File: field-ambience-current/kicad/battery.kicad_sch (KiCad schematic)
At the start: 10 parts, among them J4 SWD 1.27mm (SWCLK/GND/SWDIO), SW11 Reset 6mm SMD, SW12 BOOTSEL 6mm SMD (DNP for THT-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, U1 Raspberry_Pi_Pico2 (RP2350)

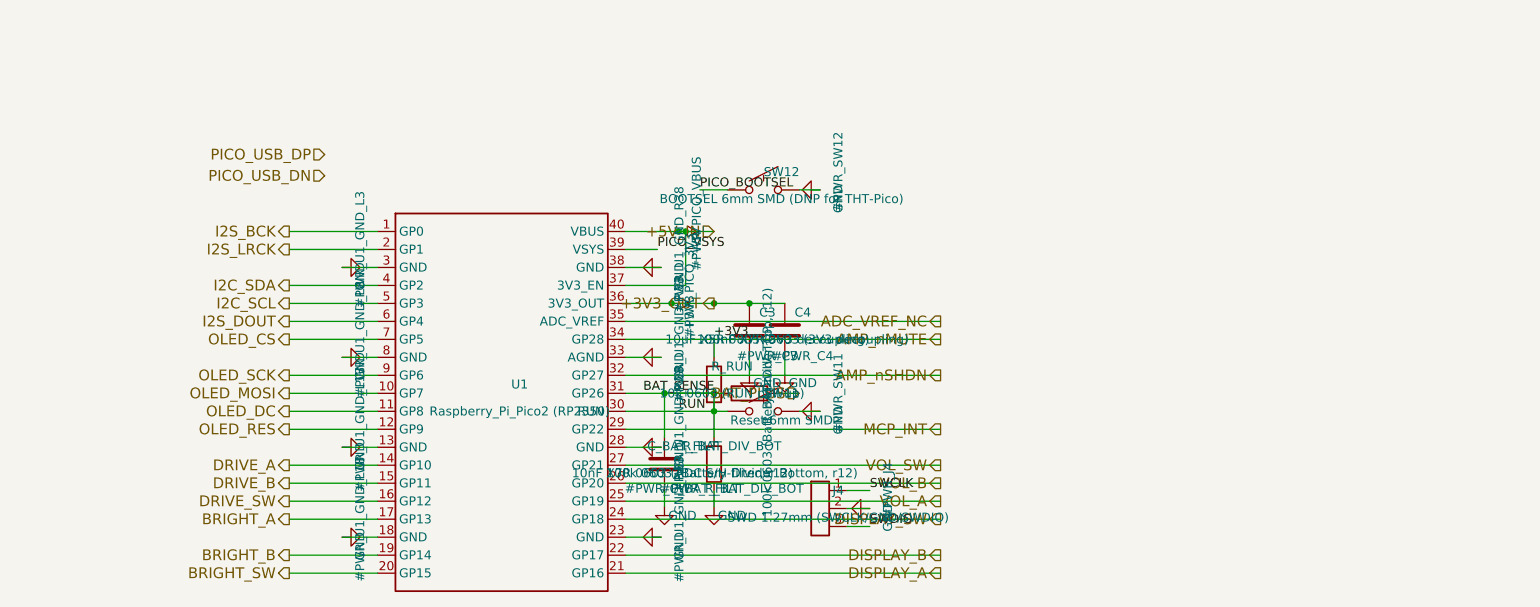
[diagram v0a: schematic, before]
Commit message: pcb(gen): r12-Sense + r9-Battery — KiCad-Generator vervollständigt
Zweite + dritte Hälfte von r10-B9/r7-B3. Bringt Generator vollständig in
Sync mit allen SPEC-Revisionen r9 (Battery-Add), r12 (Battery-Sense-HW),
r10-LED (LED1 auf PCA-Ch 10).

5 neue Library-Symbole (zwischen _pca9685pw_lib_symbol und
_rotary_encoder_switch_lib_symbol):
- _mcp73831_lib_symbol() — SOT-23-5, 5-pin Microchip-Charger
- _tps61089_lib_symbol() — QFN-12+ePAD, 13-pin TI-Boost
- _dmg2305ux_lib_symbol() — SOT-23, 3-pin P-MOSFET
- _inductor_lib_symbol() — Device:L, 2-pin
- _schottky_diode_lib_symbol() — Device:D_Schottky, 2-pin

Neuer Sheet 7 battery.kicad_sch (106 KB, 1848 Zeilen, paren-balanced):
- U7 MCP73831 LiPo-Charger 500mA via R21=2kΩ R_PROG, STAT→R_CHRG→LED_CHRG→+5V
- U8 TPS61089 Boost LiPo→5V mit L1 2.2µH + R23/R24 FB-Divider (200k/39k → ~4.92V)
- Q1 DMG2305UX P-MOS Power-Path (S=VBUS_USBC, D=+5V_OUT, G→R22 10kΩ pull-down)
- D3 SS34 Schottky zwischen BOOST_OUT und +5V_OUT (Reverse-Protect)
- J9 JST-PH-2P, C_BAT_IN/HF (22µF+100nF), C_BOOST_OUT/HF (22µF+100nF)
- Hier-I/O: VBUS_USBC ← (Power-Tree), BAT_PLUS → (Pico), +5V_OUT → (System-Rail)

r12-Sense in pico_sheet:
- GP26 STATUS_LED-Block entfernt (R19+LED1+GND-Flag weg, 0 hits in pico.kicad_sch)
- BAT_SENSE-Divider rein: R_BAT_DIV_TOP/BOT (100kΩ je), C_BAT_FILT (10nF)
- Hier-Input BAT_PLUS am Divider-Top

r12-Sense in mcp_sheet:
- GPA7 NC_GPA7 → USB_VBUS_SENSE mit R_VBUS_SENSE (10kΩ Series) + R_VBUS_PD
  (100kΩ Pull-Down) + hier-Input VBUS_USBC
- LED1 + R_LED_STATUS (390Ω 0603) auf PCA-Ch 10 (Pin 17, rechts) bei (130, 230)
- STATUS_LED_K Net-Label matched LED1-Kathode mit PCA-LED10-Pin
- NC-Loop reduziert auf LED11-LED15

power_tree_sheet:
- VBUS_USBC hier-Output (90° nach oben) am pre-fuse Rail-Tap bei (30.48, RAIL_Y-6)

root_sheet:
- Sheet 7 Battery-Block bei (30, 180) size 60×40 mit Pins VBUS_USBC/BAT_PLUS/+5V_OUT
- Existing Sheet-Blöcke erweitert: power_tree +VBUS_USBC out (90,95), pico +BAT_PLUS
  in (130,165), mcp +VBUS_USBC in 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
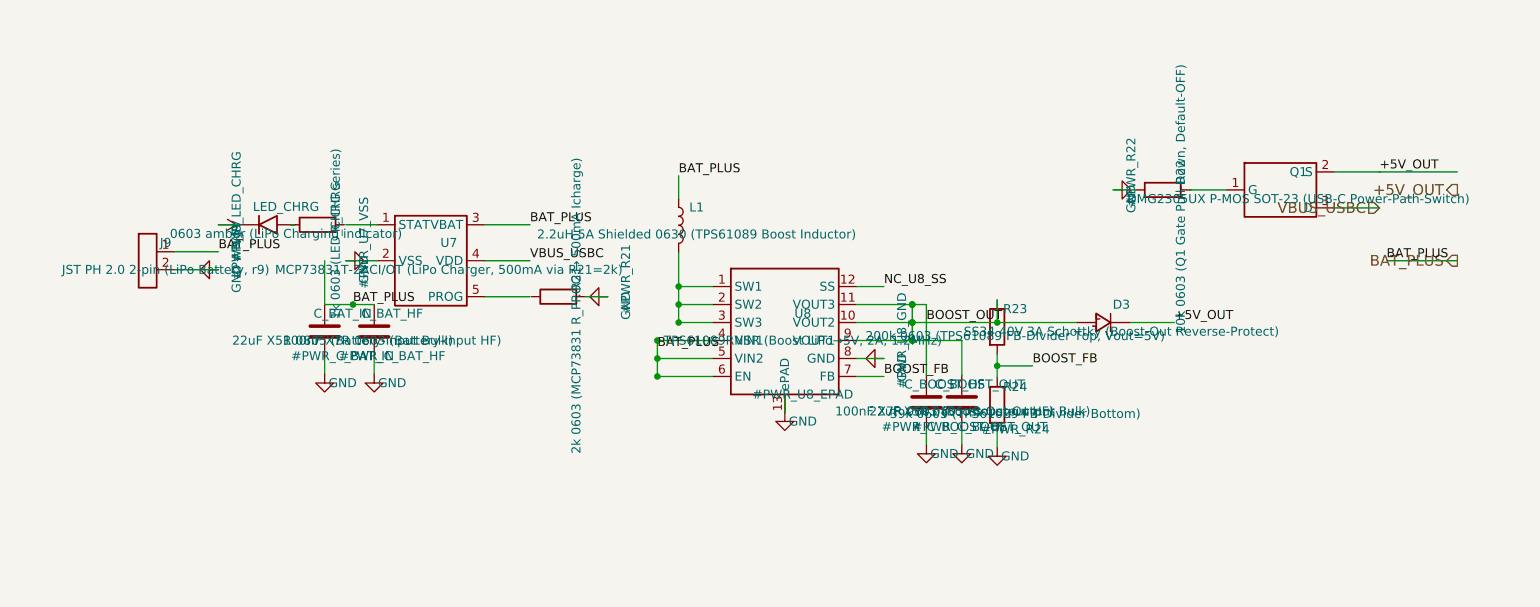
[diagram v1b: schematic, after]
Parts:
- removed C3: 10uF X5R 0805 (3V3 decoupling), Capacitor_SMD:C_0805_2012Metric, symbol Device:C
- removed C4: 100nF X7R 0603 (3V3 decoupling), Capacitor_SMD:C_0603_1608Metric, symbol Device:C
- removed C_BAT_FILT: 10nF X7R 0603 (ADC S/H filter, r12), Capacitor_SMD:C_0603_1608Metric, symbol Device:C
- removed J4: SWD 1.27mm (SWCLK/GND/SWDIO), Connector_PinHeader_1.27mm:PinHeader_1x03_P1.27mm_Vertical, symbol Connector:Conn_01x03
- removed R_BAT_DIV_BOT: 100k 0603 (Battery-Divider Bottom, r12), Resistor_SMD:R_0603_1608Metric, symbol Device:R
- removed R_BAT_DIV_TOP: 100k 0603 (Battery-Divider Top, r12), Resistor_SMD:R_0603_1608Metric, symbol Device:R
- removed R_RUN: 10k 0603 (RUN pull-up), Resistor_SMD:R_0603_1608Metric, symbol Device:R
- removed SW11: Reset 6mm SMD, Button_Switch_SMD:SW_SPST_TL3342, symbol Switch:SW_Push
- removed SW12: BOOTSEL 6mm SMD (DNP for THT-Pico), Button_Switch_SMD:SW_SPST_TL3342, symbol Switch:SW_Push
- removed U1: Raspberry_Pi_Pico2 (RP2350), MCU_Module:RPi_Pico_SMD_TH, symbol MCU:Pico2
- added C_BAT_HF: 100nF X7R 0603 (Battery-Input HF), Capacitor_SMD:C_0603_1608Metric, symbol Device:C
- added C_BAT_IN: 22uF X5R 0805 (Battery-Input Bulk), Capacitor_SMD:C_0805_2012Metric, symbol Device:C
- added C_BOOST_HF: 100nF X7R 0603 (Boost-Output HF), Capacitor_SMD:C_0603_1608Metric, symbol Device:C
- added C_BOOST_OUT: 22uF X5R 0805 (Boost-Output Bulk), Capacitor_SMD:C_0805_2012Metric, symbol Device:C
- added D3: SS34 40V 3A Schottky (Boost-Out Reverse-Protect), Diode_SMD:D_SMA, symbol Device:D_Schottky
- added J9: JST PH 2.0 2-pin (LiPo Battery, r9), Connector_JST:JST_PH_S2B-PH-SM4-TB_1x02-1MP_P2.00mm_Horizontal, symbol Connector:Conn_01x02
- added L1: 2.2uH 5A Shielded 0630 (TPS61089 Boost Inductor), Inductor_SMD:L_0630_6.0x6.0mm, symbol Device:L
- added LED_CHRG: 0603 amber (LiPo Charging indicator), LED_SMD:LED_0603_1608Metric, symbol Device:LED
- added Q1: DMG2305UX P-MOS SOT-23 (USB-C Power-Path-Switch), Package_TO_SOT_SMD:SOT-23, symbol Transistor_FET:DMG2305UX
- added R21: 2k 0603 (MCP73831 R_PROG → 500mA Icharge), Resistor_SMD:R_0603_1608Metric, symbol Device:R
- added R22: 10k 0603 (Q1 Gate Pull-Down, Default-OFF), Resistor_SMD:R_0603_1608Metric, symbol Device:R
- added R23: 200k 0603 (TPS61089 FB-Divider Top, Vout=5V), Resistor_SMD:R_0603_1608Metric, symbol Device:R
- added R24: 39k 0603 (TPS61089 FB-Divider Bottom), Resistor_SMD:R_0603_1608Metric, symbol Device:R
- added R_CHRG: 1k 0603 (LED_CHRG series), Resistor_SMD:R_0603_1608Metric, symbol Device:R
- added U7: MCP73831T-2ACI/OT (LiPo Charger, 500mA via R21=2k), Package_TO_SOT_SMD:SOT-23-5, symbol Battery:MCP73831
- added U8: TPS61089RNSR (Boost LiPo→5V, 2A, 1.2MHz), Package_DFN_QFN:VQFN-12-1EP_3x3mm_P0.5mm_EP1.5x1.5mm, symbol Regulator_Switching:TPS61089
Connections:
- net +5V: now also LED_CHRG.1 (K)
- net BAT_PLUS: now also C_BAT_HF.1, C_BAT_IN.1, J9.1 (Pin_1), L1.1, U7.3 (VBAT), U8.4 (VIN1), U8.5 (VIN2), U8.6 (EN)
- net GND: now also C_BAT_HF.2, C_BAT_IN.2, C_BOOST_HF.2, C_BOOST_OUT.2, J9.2 (Pin_2), R21.2, R22.1, R24.2, U7.2 (VSS), U8.13 (ePAD), U8.8 (GND)
- new net: L1.2, U8.1 (SW1), U8.2 (SW2), U8.3 (SW3)
- new net: Q1.1 (G), R22.2
- new net: LED_CHRG.2 (A), R_CHRG.1
- new net +5V_OUT: D3.1 (K), Q1.2 (S)
- new net BOOST_FB: R23.2, R24.1, U8.7 (FB)
- new net BOOST_OUT: C_BOOST_HF.1, C_BOOST_OUT.1, D3.2 (A), R23.1, U8.10 (VOUT2), U8.11 (VOUT3), U8.9 (VOUT1)
- new net NC_U8_SS: U8.12 (SS)
- new net VBUS_USBC: Q1.3 (D), U7.4 (VDD)
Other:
- title: Field Ambience PCB — Sheet 2: Pico 2 (RP2350) -> Field Ambience PCB — Sheet 7: Battery & Power-Path (r9 + r12)

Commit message: pcb(gen): kicad-Analyzer-Bugfixes (ERC: 8 errors→6, NT-001 33→16)
Schematic-Analyzer fand drei klassen von echten Connectivity-Bugs in den
beiden Generator-Catchup-Commits (50b5e02 + 0a3a740). Alle gefixt.

Bug 1: Label-Position 3mm neben Wire-Endpunkt → 33 dangling-pin-Nets
  - r10-LED PCA-pin-Labels (10 LEDs + 5 NC + STATUS_LED_K) saßen bei
    PCA_PIN_*_X±8 statt ±5 → keine 10 LEDs waren physisch an PCA9685
    connected. Fix: Labels auf Wire-Endpunkt verschoben.

Bug 2: Sub-mm-Gaps (0.19mm) zwischen Wires und Resistor-Pins
  - R rotation=90 horizontal hat pin1/pin2 bei sx±3.81 (X.19/X.81).
    Meine Wires endeten bei integer-mm → 0.19mm Gap = dangling.
  - Fixed: R_OE (mcp_sheet PCA-OE), R_VBUS_SENSE (mcp_sheet GPA7),
    R_CHRG (battery_sheet U7-STAT), R21 (battery_sheet U7-PROG).

Bug 3: Y-Inversion bei Q1 DMG2305UX P-MOS
  - KiCad-Symbol-local-Y ist invertiert zu Schematic-abs-Y. Meine
    q1_s_y und q1_d_y waren vertauscht → Q1.2 (S) auf +5V_OUT statt
    VBUS_USBC (SPEC-§2.2-violation!). Analyzer hat das korrekt
    gefangen. Fix: Y-Werte getauscht, S=VBUS_USBC ✓, D=+5V_OUT ✓.

Bug 4: Lokal-Label statt Hier-Label für Cross-Sheet-Nets
  - Lokale Labels mergen NICHT mit Hier-Labels im Analyzer-View
    (auch wenn KiCad-GUI das toleriert). Battery_sheet U7-VDD,
    U7-VBAT, U8-VIN, L1-top, Q1-D, D3-K, J9-pin1, C_BAT_IN waren
    alle mit lokalen Labels markiert → keine Cross-Sheet-Merge.
    Plus mcp_sheet PCA-side I²C-SCL/SDA.
  - Fix: alle zu hier_labels umgewandelt. I²C-Bus hat jetzt 4 Pins
    (U1+U2+R-Pullup+U6) statt 2 isolierte Sub-Nets.

Bug 5: +5V_OUT (Battery) mergt nicht mit System +5V
  - Hier-Label-Name "+5V_OUT" ≠ Power-Tree-Net-Name "+5V". Battery's
    +5V_OUT war ein isoliertes 2-pin Net (D3.K + Q1.D).
  - Fix: Bridge-Label "+5V_OUT" am existing Power-Tree→Pico-Wire
    (110, 50) im root_sheet. +5V hat jetzt 49 pins (war 47).

Bug 6: Redundante Edge-Hier-Labels in battery_sheet
  - Hatte standalone hier_labels bei (235, 70/80) zusätzlich zu de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
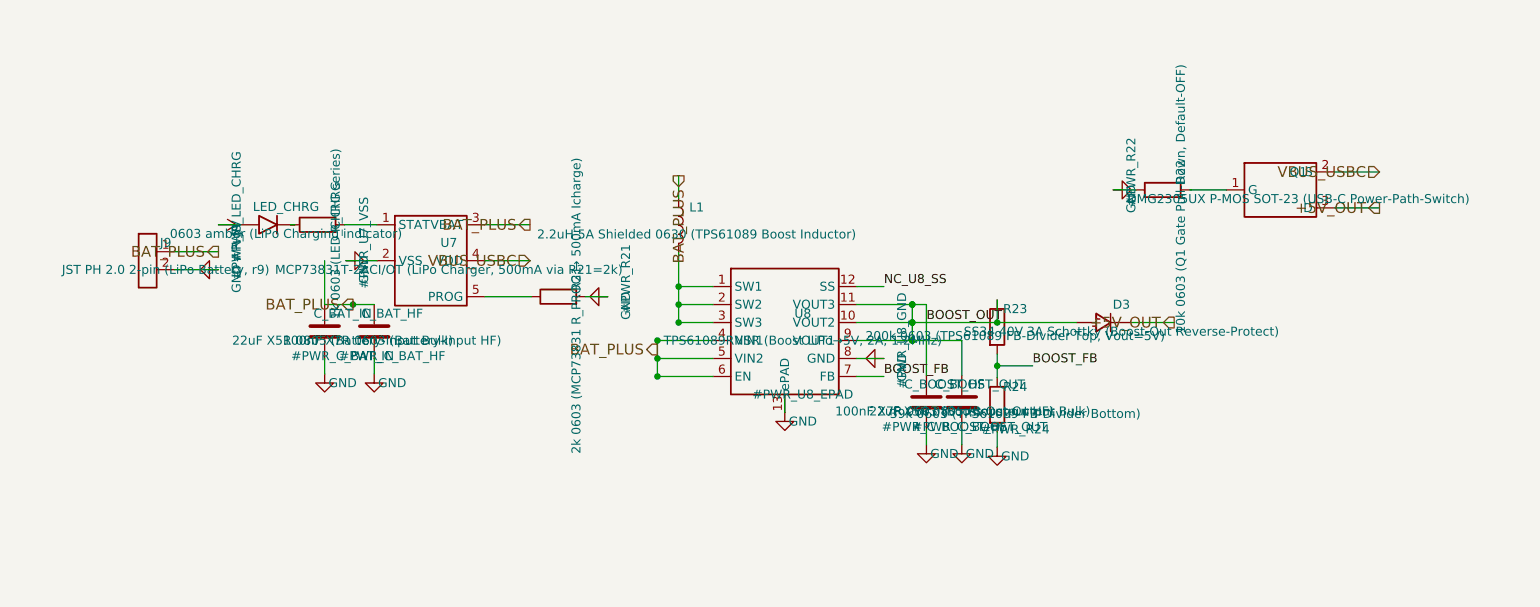
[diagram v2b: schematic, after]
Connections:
- net +5V: now also LED_CHRG.2 (A); no longer LED_CHRG.1 (K)
- net +5V_OUT: now also Q1.3 (D); no longer Q1.2 (S)
- net VBUS_USBC: now also Q1.2 (S); no longer Q1.3 (D)
- net at R21.1: now also U7.5 (PROG)
- net at R_CHRG.1: now also LED_CHRG.1 (K); no longer LED_CHRG.2 (A)
- net at R_CHRG.2: now also U7.1 (STAT)
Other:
- moved on the sheet: LED_CHRG
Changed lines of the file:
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@@
       (project "field_ambience"
         (path "/f6a664dc-7032-4108-a10b-e4076008e6bd" (reference "R_CHRG") (unit 1)))))
-  (symbol (lib_id "Device:LED") (at 67.0 74.92 0) (unit 1)
+  (symbol (lib_id "Device:LED") (at 67.0 74.92 180) (unit 1)
     (in_bom yes) (on_board yes) (dnp no)
       (property "Reference" "LED_CHRG" (at 69.54 72.38 0)
@@
     (stroke (width 0) (type default))
 )
-  (wire (pts (xy 82.38 74.92) (xy 78.0 74.92))
+  (wire (pts (xy 82.38 74.92) (xy 77.81 74.92))
     (stroke (width 0) (type default))
 )
@@
     (stroke (width 0) (type default))
 )
-  (wire (pts (xy 97.62 85.08) (xy 104.0 85.08))
+  (wire (pts (xy 97.62 85.08) (xy 104.19 85.08))
     (stroke (width 0) (type default))
 )
@@
     (stroke (width 0) (type default))
 )
+  (wire (pts (xy 217.62 67.46) (xy 224.0 67.46))
+    (stroke (width 0) (type default))
+)
   (wire (pts (xy 217.62 72.54) (xy 224.0 72.54))
     (stroke (width 0) (type default))
 )
-  (wire (pts (xy 217.62 67.46) (xy 224.0 67.46))
-    (stroke (width 0) (type default))
-)
-  (wire (pts (xy 224.0 67.46) (xy 235 67.46))
-    (stroke (width 0) (type default))
-)
-  (wire (pts (xy 225 80) (xy 235 80))
-    (stroke (width 0) (type default))
-)
   (junction (at 79 86.19) (diameter 0) (color 0 0 0 0)
 )
@@
 )
   (junction (at 170 88.73) (diameter 0) (color 0 0 0 0)
-)
-  (label "BAT_PLUS" (at 60 78.73 0) (fields_autoplaced)
-    (effects (font (size 1.27 1.27)) (justify left bottom))
-)
-  (label "VBUS_USBC" (at 104.0 80.0 0) (fields_autoplaced)
-    (effects (font (size 1.27 1.27)) (justify left bottom))
-)
-  (label "BAT_PLUS" (at 104.0 74.92 0) (fields_autoplaced)
-    (effects (font (size 1.27 1.27)) (justify left bottom))
-)
-  (label "BAT_PLUS" (at 79 86.19 0) (fields_autoplaced)
-    (effects (font (size 1.27 1.27)) (justify left bottom))
-)
-  (label "BAT_PLUS" (at 125 68 0) (fields_autoplaced)
-    (effects (font (size 1.27 1.27)) (justify left bottom))
-)
-  (label "BAT_PLUS" (at 122 92.54 0) (fields_autoplaced)
-    (effects (font (size 1.27 1.27)) (justify left bottom))
 )
   (label "BOOST_OUT" (at 160 88.73 0) (fields_autoplaced)
@@
     (effects (font (size 1.27 1.27)) (justify left bottom))
 )
-  (label "+5V_OUT" (at 195 88.73 0) (fields_autoplaced)
-    (effects (font (size 1.27 1.27)) (justify left bottom))
-)
-  (label "+5V_OUT" (at 224.0 67.46 0) (fields_autoplaced)
-    (effects (font (size 1.27 1.27)) (justify left bottom))
-)
-  (label "BAT_PLUS" (at 225 80 0) (fields_autoplaced)
-    (effects (font (size 1.27 1.27)) (justify left bottom))
-)
-  (hierarchical_label "VBUS_USBC" (shape input) (at 224.0 72.54 180)
-    (effects (font (size 1.524 1.524)) (justify right))
-)
-  (hierarchical_label "+5V_OUT" (shape output) (at 235 70 0)
-    (effects (font (size 1.524 1.524)) (justify right))
-)
-  (hierarchical_label "BAT_PLUS" (shape output) (at 235 80 0)
-    (effects (font (size 1.524 1.524)) (justify right))
-)
+  (hierarchical_label "BAT_PLUS" (shape output) (at 60 78.73 0)
+    (effects (font (size 1.524 1.524)) (justify right))
+)
+  (hierarchical_label "VBUS_USBC" (shape input) (at 104.0 80.0 0)
+    (effects (font (size 1.524 1.524)) (justify right))
+)
+  (hierarchical_label "BAT_PLUS" (shape output) (at 104.0 74.92 0)
+    (effects (font (size 1.524 1.524)) (justify right))
+)
+  (hierarchical_label "BAT_PLUS" (shape output) (at 79 86.19 0)
+    (effects (font (size 1.524 1.524)) (justify right))
+)
+  (hierarchical_label "BAT_PLUS" (shape output) (at 125 68 90)
+    (effects (font (size 1.524 1.524)) (justify right))
+)
+  (hierarchical_label "BAT_PLUS" (shape output) (at 122 92.54 180)
+    (effects (font (size 1.524 1.524)) (justify right))
+)
+  (hierarchical_label "+5V_OUT" (shape output) (at 195 88.73 0)
+    (effects (font (size 1.524 1.524)) (justify right))
+)
+  (hierarchical_label "VBUS_USBC" (shape input) (at 224.0 67.46 180)
+    (effects (font (size 1.524 1.524)) (justify right))
+)
+  (hierarchical_label "+5V_OUT" (shape output) (at 224.0 72.54 0)
+    (effects (font (size 1.524 1.524)) (justify right))
+)

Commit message: pcb(bom): r12-B12 — 9 falsche LCSC-Codes via jlcsearch-Audit korrigiert + r12-B11 TPS-Package-Blocker
JLC-Pricing-Estimate-Run hat 9 falsche LCSC-Codes im Generator aufgedeckt.
Alle MPN-Strings waren korrekt, aber die zugewiesenen LCSC-Codes pointed
auf völlig andere Teile. Bei sofortiger JLC-Bestellung wäre der Prototyp
DOA gewesen (BAT_SENSE-Divider 130Ω/130Ω statt 100k/100k, Boost-FB 15Ω/0.21k
statt 200k/39k, alle LEDs nicht-existent, etc.).

Korrigierte Mappings (via jlcsearch-API-Verifikation):
- 100kΩ 0603 (R_BAT_DIV_TOP/BOT, R_VBUS_PD): C22796 → C25803 (Basic)
- 200kΩ 0603 (R23): C22810 → C25811 (Basic)
- 39kΩ 0603 (R24): C25090 → C23153 (Basic)
- 390Ω 0603 (R_LED6-15, R_LED_STATUS): C23289 → C23151 (Basic)
- MCP73831T-2ACI/OT (U7): C14879 → C424093 (Extended)
- DMG2305UX-7 (Q1): C147074 → C150470 (Extended)
- SWPA6045S2R2MT (L1): C32330 → C83455 (Extended)
- S2B-PH-SM4-TB SMD (J9): C146061 → C295747 (Extended)
- 0603 white LED (LED1, LED6-15): C72043 → C965808 XL-1608UWC-04 (Extended)

Neuer BLOCKER r12-B11: TPS61089-Package-Mismatch
SPEC §2.2 spezifiziert TPS61089RNSR (QFN-12 3×3mm), aber LCSC hat nur
TPS61089RNRR (VQFN-11 2×2.5mm HotRod, anderer Footprint + Pinout).
Generator markiert LCSC vorerst als "TBD-USER-SUPPLY-or-RNRR-refactor"
bis User-Decision. 3 Lösungswege in PCB_TODO r12-B11 dokumentiert
(RNRR-Refactor / RNSR-Konsignierung / Hand-Solder).

Side-Effekt: 4 der korrigierten Resistor-SKUs sind Basic (kein Extended-
Setup-Fee) → spart $12 bei 5-Boards. Extended-SKU-Count 23 → 19.

JLC-Cost-Estimate aktualisiert in CHANGELOG: 5 Prototyp-Boards ~$567
(JLC $294 + User-Supplied $272 + Battery/OLED/Choc/Pico/Speaker), per
Board ~$113. Bei 100 Stück ~$6884 (~$69/Board).

Generator/SPEC/PCB_TODO/CHANGELOG synchron. Analyzer-Status unverändert
(LCSC sind Metadata, keine Connectivity-Änderung).

https://claude.ai/code/session_01K5kLTFpDCCoYwx2dq6RkAv
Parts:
- J9: LCSC C146061 -> C295747; MPN S2B-PH-SM4-TB -> S2B-PH-SM4-TB(LF)(SN)
- L1: LCSC C32330 -> C83455
- Q1: LCSC C147074 -> C150470
- R23: LCSC C22810 -> C25811
- R24: LCSC C25090 -> C23153
- U7: LCSC C14879 -> C424093
- U8: LCSC C2671 -> TBD-USER-SUPPLY-or-RNRR-refactor
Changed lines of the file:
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@@
       (property "Datasheet" "~" (at 50 80 0)
         (effects (font (size 1.27 1.27)) hide))
-      (property "MPN" "S2B-PH-SM4-TB" (at 52.54 83.81 0)
-        (effects (font (size 1.27 1.27)) hide))
-      (property "LCSC" "C146061" (at 52.54 85.08 0)
+      (property "MPN" "S2B-PH-SM4-TB(LF)(SN)" (at 52.54 83.81 0)
+        (effects (font (size 1.27 1.27)) hide))
+      (property "LCSC" "C295747" (at 52.54 85.08 0)
         (effects (font (size 1.27 1.27)) hide))
     (instances
@@
       (property "MPN" "MCP73831T-2ACI/OT" (at 92.54 83.81 0)
         (effects (font (size 1.27 1.27)) hide))
-      (property "LCSC" "C14879" (at 92.54 85.08 0)
+      (property "LCSC" "C424093" (at 92.54 85.08 0)
         (effects (font (size 1.27 1.27)) hide))
     (instances
@@
       (property "MPN" "TPS61089RNSR" (at 142.54 93.81 0)
         (effects (font (size 1.27 1.27)) hide))
-      (property "LCSC" "C2671" (at 142.54 95.08 0)
+      (property "LCSC" "TBD-USER-SUPPLY-or-RNRR-refactor" (at 142.54 95.08 0)
         (effects (font (size 1.27 1.27)) hide))
     (instances
@@
       (property "MPN" "SWPA6045S2R2MT" (at 127.54 78.81 0)
         (effects (font (size 1.27 1.27)) hide))
-      (property "LCSC" "C32330" (at 127.54 80.08 0)
+      (property "LCSC" "C83455" (at 127.54 80.08 0)
         (effects (font (size 1.27 1.27)) hide))
     (instances
@@
       (property "MPN" "0603WAF2003T5E" (at 172.54 93.16000000000001 0)
         (effects (font (size 1.27 1.27)) hide))
-      (property "LCSC" "C22810" (at 172.54 94.43 0)
+      (property "LCSC" "C25811" (at 172.54 94.43 0)
         (effects (font (size 1.27 1.27)) hide))
     (instances
@@
       (property "MPN" "0603WAF3902T5E" (at 172.54 104.16000000000001 0)
         (effects (font (size 1.27 1.27)) hide))
-      (property "LCSC" "C25090" (at 172.54 105.43 0)
+      (property "LCSC" "C23153" (at 172.54 105.43 0)
         (effects (font (size 1.27 1.27)) hide))
     (instances
@@
       (property "MPN" "DMG2305UX-7" (at 212.54 73.81 0)
         (effects (font (size 1.27 1.27)) hide))
-      (property "LCSC" "C147074" (at 212.54 75.08 0)
-        (effects (font (size 1.27 1.27)) hide))
-    (instances
+      (property "LCSC" "C150470" (at 212.54 75.08 0)
+        (effects (font (size 1.27 1.27)) hide))
+    (instances
